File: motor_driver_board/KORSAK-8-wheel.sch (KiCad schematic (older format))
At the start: 15 parts, among them J1 Screw_Terminal_01x06, J2 Conn_01x02_Male, J3 Screw_Terminal_01x06, M1 Motor_DC, M2 Motor_DC, M3 Motor_DC, M4 Motor_DC, M5 Motor_DC, M6 Motor_DC, M7 Motor_DC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

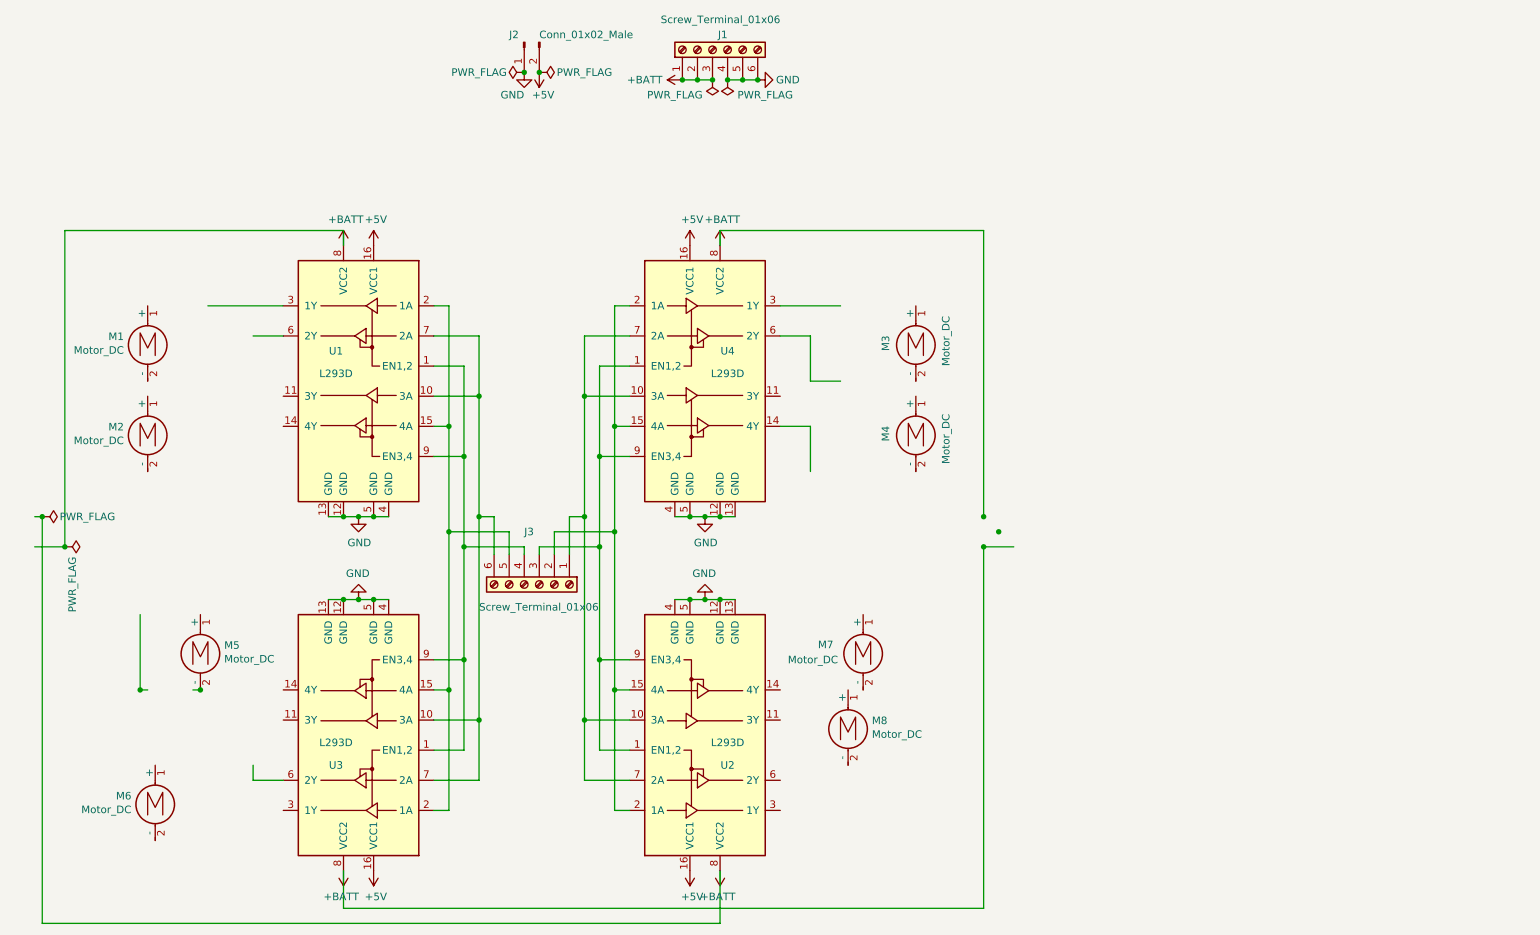
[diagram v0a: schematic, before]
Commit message: Добавил конденсаторы в схему и исправил её
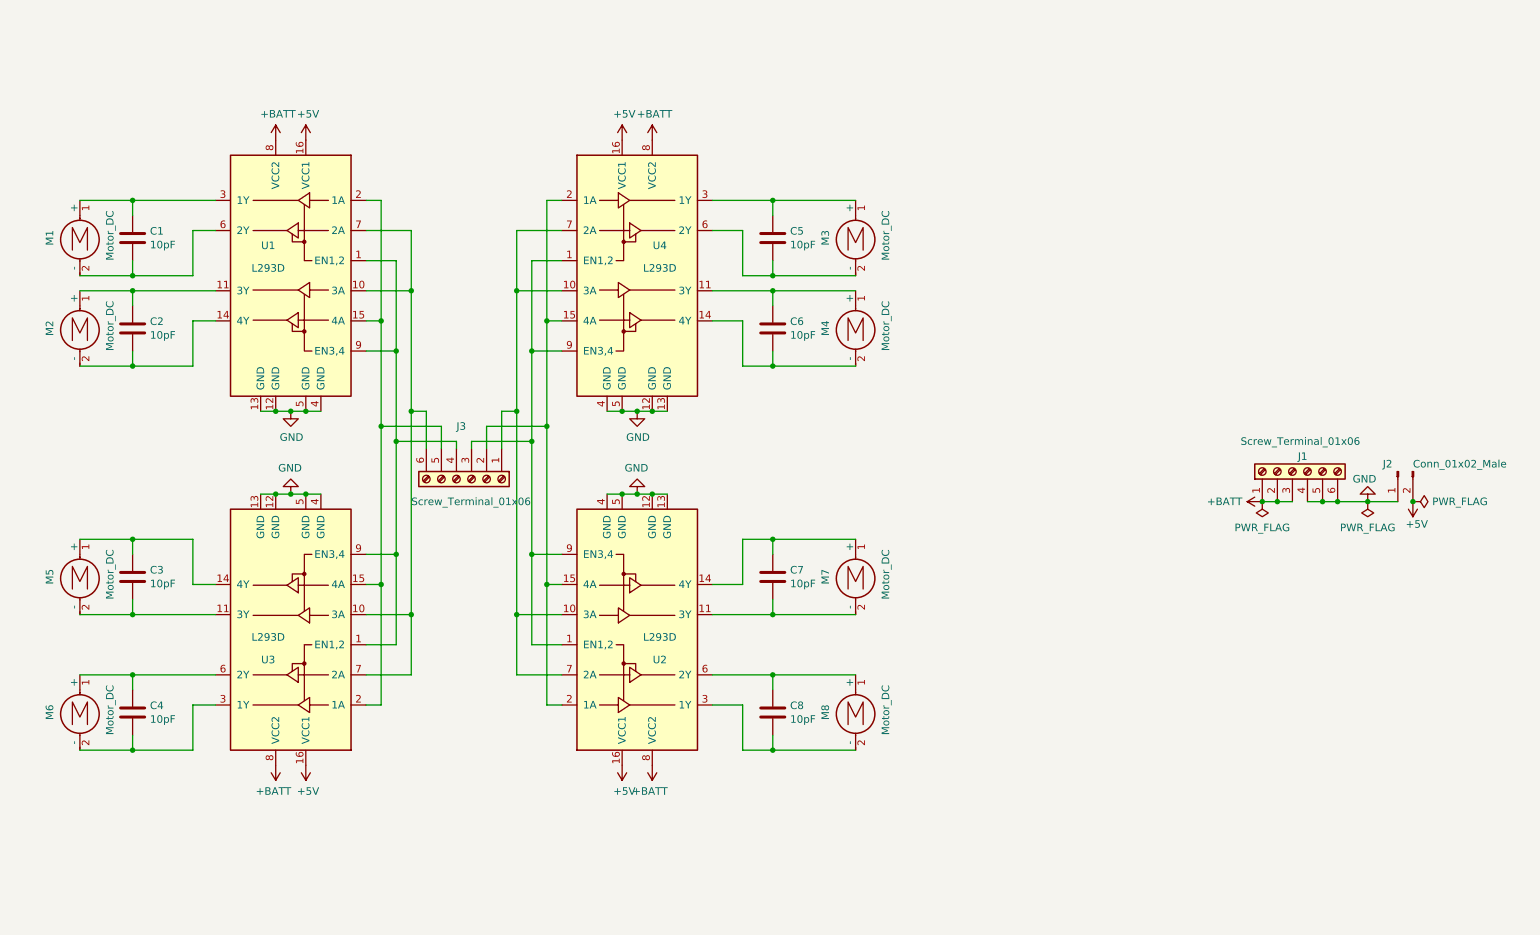
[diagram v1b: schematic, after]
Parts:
- added C1, C2, C3, C4, C5, C6, C7, C8: 10pF, Capacitor_THT:C_Disc_D5.0mm_W2.5mm_P5.00mm, symbol Device:C
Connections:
- wire segments 108 -> 146
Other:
- moved on the sheet: J1, J2, J3, M1, M2, M3, M4, M5, M6, M7, M8, U1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

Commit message: Добавил выводы под выключатель и индикатор заряда
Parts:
- added J4: Charge Indicator, TerminalBlock_Phoenix:TerminalBlock_Phoenix_MKDS-1,5-2_1x02_P5.00mm_Horizontal, symbol Connector:Screw_Terminal_01x02
- added SW1: SW_SPST, TerminalBlock_Phoenix:TerminalBlock_Phoenix_MKDS-1,5-2_1x02_P5.00mm_Horizontal, symbol Switch:SW_SPST
- J1: value Screw_Terminal_01x06 -> Battery
- J2: value Conn_01x02_Male -> 5V connector
- J3: value Screw_Terminal_01x06 -> Logic
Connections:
- net +5V: now also J2.1 (Pin_1); no longer J2.2 (Pin_2)
- net +BATT: now also J4.2 (Pin_2)
- net GND: now also SW1.2 (B); no longer J1.4 (Pin_4), J1.5 (Pin_5), J1.6 (Pin_6), J2.1 (Pin_1)
- new net: J1.4 (Pin_4), J1.5 (Pin_5), J1.6 (Pin_6), J2.2 (Pin_2), J4.1 (Pin_1), SW1.1 (A)
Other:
- note added: "+"
- note added: "-"
- moved on the sheet: J2
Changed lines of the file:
@@
 Title "KORSAK Motor Driver board"
 Date "2021-03-13"
-Rev "5"
+Rev "6"
 Comp ""
 Comment1 ""
@@
 L power:GND #PWR04
 U 1 1 5FFD08AA
-P 9750 4350
-F 0 "#PWR04" H 9750 4100 50  0001 C CNN
-F 1 "GND" H 9850 4200 50  0000 R CNN
-F 2 "" H 9750 4350 50  0001 C CNN
-F 3 "" H 9750 4350 50  0001 C CNN
-	1    9750 4350
-	-1   0    0    1
+P 10200 4800
+F 0 "#PWR04" H 10200 4550 50  0001 C CNN
+F 1 "GND" V 10200 4650 50  0000 R CNN
+F 2 "" H 10200 4800 50  0001 C CNN
+F 3 "" H 10200 4800 50  0001 C CNN
+	1    10200 4800
+	0    -1   -1   0
 $EndComp
 $Comp
@@
 U 1 1 60435B47
 P 9950 4150
-F 0 "J2" V 9900 4250 50  0000 R CNN
-F 1 "Conn_01x02_Male" V 9900 4050 50  0000 R CNN
+F 0 "J2" V 9900 4150 50  0000 R CNN
+F 1 "5V connector" V 10000 4700 50  0000 R CNN
 F 2 "Connector_PinHeader_2.54mm:PinHeader_1x02_P2.54mm_Horizontal" H 9950 4150 50  0001 C CNN
 F 3 "~" H 9950 4150 50  0001 C CNN
 	1    9950 4150
-	0    -1   1    0
+	0    1    1    0
 $EndComp
 Wire Wire Line
@@
 P 3800 4200
 F 0 "J3" V 3450 4100 50  0000 L CNN
-F 1 "Screw_Terminal_01x06" V 3950 3800 50  0000 L CNN
+F 1 "Logic" V 3900 4050 50  0000 L CNN
 F 2 "TerminalBlock_Phoenix:TerminalBlock_Phoenix_MKDS-1,5-6_1x06_P5.00mm_Horizontal" H 3800 4200 50  0001 C CNN
 F 3 "~" H 3800 4200 50  0001 C CNN
@@
 P 9250 4150
 F 0 "J1" V 9350 4050 50  0000 L CNN
-F 1 "Screw_Terminal_01x06" V 9450 3700 50  0000 L CNN
+F 1 "Battery" V 9450 3950 50  0000 L CNN
 F 2 "TerminalBlock_Phoenix:TerminalBlock_Phoenix_MKDS-1,5-6_1x06_P5.00mm_Horizontal" H 9250 4150 50  0001 C CNN
 F 3 "~" H 9250 4150 50  0001 C CNN
@@
 P 9050 4350
 F 0 "#FLG0101" H 9050 4425 50  0001 C CNN
-F 1 "PWR_FLAG" H 9050 4523 50  0000 C CNN
+F 1 "PWR_FLAG" H 9300 4450 50  0000 C CNN
 F 2 "" H 9050 4350 50  0001 C CNN
 F 3 "~" H 9050 4350 50  0001 C CNN
@@
 	0    1    1    0
 $EndComp
-Connection ~ 10050 4350
 $Comp
 L power:PWR_FLAG #FLG0103
 U 1 1 60AE12BA
-P 9750 4350
-F 0 "#FLG0103" H 9750 4425 50  0001 C CNN
-F 1 "PWR_FLAG" H 9750 4523 50  0000 C CNN
-F 2 "" H 9750 4350 50  0001 C CNN
-F 3 "~" H 9750 4350 50  0001 C CNN
-	1    9750 4350
-	-1   0    0    1
-$EndComp
-Wire Wire Line
-	9750 4350 9950 4350
+P 10200 4800
+F 0 "#FLG0103" H 10200 4875 50  0001 C CNN
+F 1 "PWR_FLAG" H 10350 4950 50  0000 C CNN
+F 2 "" H 10200 4800 50  0001 C CNN
+F 3 "~" H 10200 4800 50  0001 C CNN
+	1    10200 4800
+	1    0    0    -1
+$EndComp
+Wire Wire Line
+	9750 4350 9850 4350
+$Comp
+L Switch:SW_SPST SW1
+U 1 1 604F19B3
+P 10000 4800
+F 0 "SW1" H 10000 4900 50  0000 C CNN
+F 1 "SW_SPST" H 10000 4700 50  0001 C CNN
+F 2 "TerminalBlock_Phoenix:TerminalBlock_Phoenix_MKDS-1,5-2_1x02_P5.00mm_Horizontal" H 10000 4800 50  0001 C CNN
+F 3 "~" H 10000 4800 50  0001 C CNN
+	1    10000 4800
+	1    0    0    -1
+$EndComp
+Connection ~ 9250 4350
+Connection ~ 10200 4800
+Wire Wire Line
+	9750 4350 9750 4800
+Wire Wire Line
+	9750 4800 9800 4800
+$Comp
+L Connector:Screw_Terminal_01x02 J4
+U 1 1 6053A604
+P 9350 4550
+F 0 "J4" V 9350 4300 50  0000 L CNN
+F 1 "Charge Indicator" V 9450 4200 50  0000 L CNN
+F 2 "TerminalBlock_Phoenix:TerminalBlock_Phoenix_MKDS-1,5-2_1x02_P5.00mm_Horizontal" H 9350 4550 50  0001 C CNN
+F 3 "~" H 9350 4550 50  0001 C CNN
+	1    9350 4550
+	0    1    1    0
+$EndComp
+Connection ~ 9350 4350
+Text Notes 9350 4500 0    50   ~ 0
+-
+Text Notes 9150 4500 0    50   ~ 0
++
+Wire Wire Line
+	9950 4350 10050 4350
+Connection ~ 10050 4350
 $EndSCHEMATC

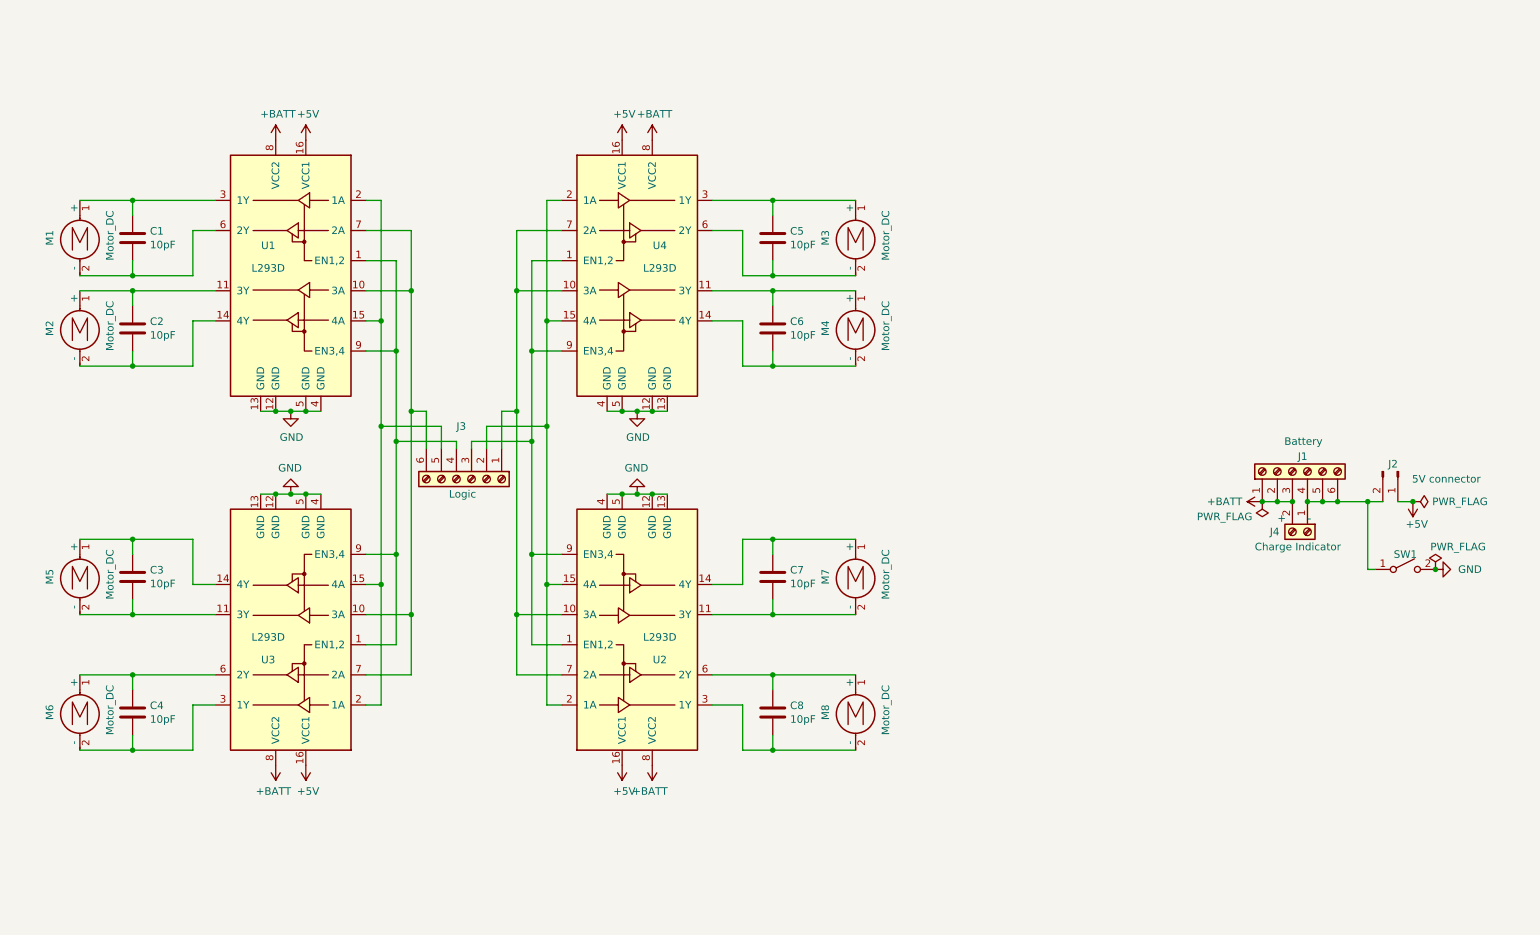
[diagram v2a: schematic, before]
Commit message: Сделал управление через логическое НЕ и метки
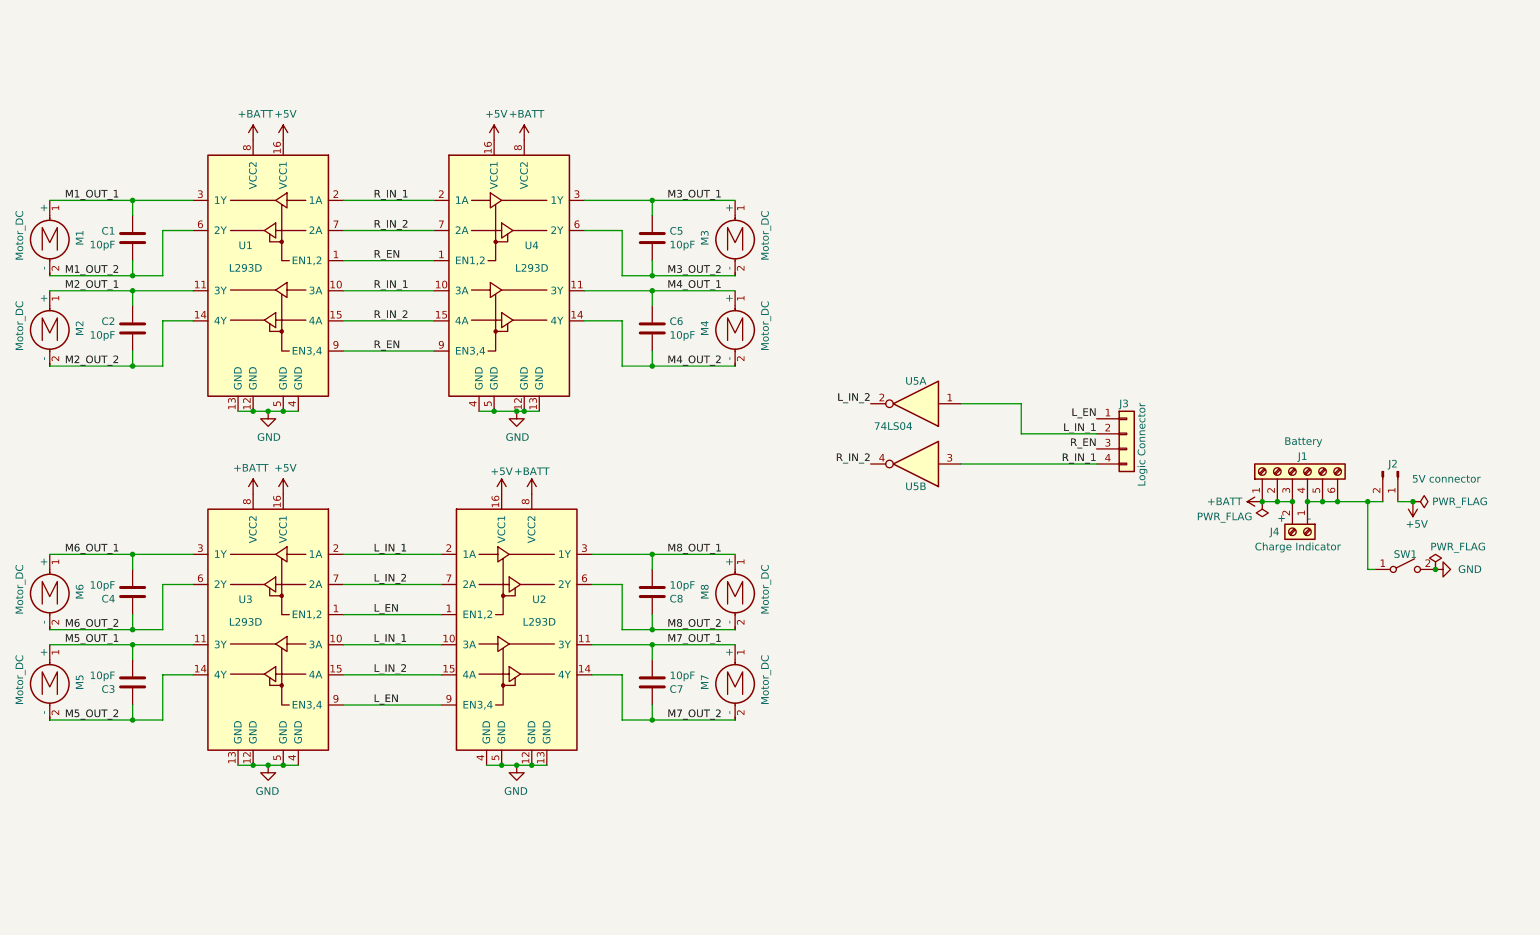
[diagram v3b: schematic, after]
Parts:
- removed J3: Logic, TerminalBlock_Phoenix:TerminalBlock_Phoenix_MKDS-1,5-6_1x06_P5.00mm_Horizontal, symbol Connector:Screw_Terminal_01x06
- added J3: Logic Connector, TerminalBlock_Phoenix:TerminalBlock_Phoenix_MKDS-1,5-4_1x04_P5.00mm_Horizontal, symbol Connector_Generic:Conn_01x04
- added U5: 74LS04, Package_DIP:DIP-14_W7.62mm_Socket_LongPads, symbol 74xx:74LS04
- U1, U2, U3, U4: footprint Package_DIP:DIP-16_W7.62mm_Socket -> Package_DIP:DIP-16_W7.62mm_Socket_LongPads
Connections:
- net L_EN: now reaches U2.1 (EN1,2), U2.9 (EN3,4)
- net L_EN: now also U3.1 (EN1,2), U3.9 (EN3,4), J3.1 (Pin_1); no longer U4.1 (EN1,2), U4.9 (EN3,4)
- net M4_OUT_1: now reaches C6.1, M4.1 (+), U4.11 (3Y)
- net M4_OUT_2: now reaches C6.2, M4.2 (-), U4.14 (4Y)
- net M3_OUT_1: now reaches C5.1, M3.1 (+), U4.3 (1Y)
- net M3_OUT_2: now reaches C5.2, M3.2 (-), U4.6 (2Y)
- net R_EN: now reaches U1.1 (EN1,2), U1.9 (EN3,4)
- net R_EN: now also U4.1 (EN1,2), U4.9 (EN3,4), J3.3 (Pin_3); no longer U3.1 (EN1,2), U3.9 (EN3,4)
- net M2_OUT_1: now reaches C2.1, M2.1 (+), U1.11 (3Y)
- net M2_OUT_2: now reaches C2.2, M2.2 (-), U1.14 (4Y)
- net M1_OUT_1: now reaches C1.1, M1.1 (+), U1.3 (1Y)
- net M1_OUT_2: now reaches C1.2, M1.2 (-), U1.6 (2Y)
- net M8_OUT_2: now reaches C8.1, U2.6 (2Y)
- net M8_OUT_2: now also M8.2 (-); no longer M8.1 (+)
- net M8_OUT_1: now reaches C8.2, U2.3 (1Y)
- net M8_OUT_1: now also M8.1 (+); no longer M8.2 (-)
- net M7_OUT_2: now reaches C7.1, U2.14 (4Y)
- net M7_OUT_2: now also M7.2 (-); no longer M7.1 (+)
- net M7_OUT_1: now reaches C7.2, U2.11 (3Y)
- net M7_OUT_1: now also M7.1 (+); no longer M7.2 (-)
- net M5_OUT_1: now reaches C3.2, U3.11 (3Y)
- net M5_OUT_1: now also M5.1 (+); no longer M5.2 (-)
- net M5_OUT_2: now reaches C3.1, U3.14 (4Y)
- net M5_OUT_2: now also M5.2 (-); no longer M5.1 (+)
- net M6_OUT_1: now reaches C4.2, U3.3 (1Y)
- net M6_OUT_1: now also M6.1 (+); no longer M6.2 (-)
- net M6_OUT_2: now reaches C4.1, U3.6 (2Y)
- net M6_OUT_2: now also M6.2 (-); no longer M6.1 (+)
- new net L_IN_1: J3.2 (Pin_2), U2.10 (3A), U2.2 (1A), U3.10 (3A), U3.2 (1A), U5.1
- new net L_IN_2: U2.15 (4A), U2.7 (2A), U3.15 (4A), U3.7 (2A), U5.2
- new net R_IN_1: J3.4 (Pin_4), U1.10 (3A), U1.2 (1A), U4.10 (3A), U4.2 (1A), U5.3
- new net R_IN_2: U1.15 (4A), U1.7 (2A), U4.15 (4A), U4.7 (2A), U5.4
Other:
- moved on the sheet: C3, C4, C5, C6, C7, C8, M1, M2, M3, M4, M5, M6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
